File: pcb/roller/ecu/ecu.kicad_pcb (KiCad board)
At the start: 4 copper layers, 187.6 x 139.6 mm, 275 parts, among them J1 SWD, J2 NTC, J3 SS-12400-004, J4 NTC, J6 TE-776163-1, J7 TE-776087-1, K1 Relay_SPDT, K10 Relay_SPST-NO, K11 Relay_SPDT, K12 Relay_SPST-NO, K13 Relay_SPDT, K14 Relay_SPST-NO, K15 Relay_SPST-NO, K16 Relay_SPST-NO, K17 Relay_SPST-NO, K18 Relay_SPST-NO, K19 Relay_SPST-NO, K2 Relay_SPDT, K20 Relay_SPST-NO, K21 Relay_SPST-NO, K22 Relay_SPST-NO, K23 Relay_SPST-NO, K24 Relay_SPDT, K25 Relay_SPST-NO, K26 Relay_SPST-NO, K27 Relay_SPST-NO, K3 Relay_SPDT, K4 Relay_SPST-NO, K5 Relay_SPDT, K6 Relay_SPST-NO, K7 Relay_SPDT, K8 Relay_SPST-NO, K9 Relay_SPDT, Q1 BSN20, Q2 NVD5C684NLT4G, Q3 NVD5C684NLT4G, Q4 BC817, Q5 BSC065N06LS5, Q6 2N7002KQ-7, Q9 BSN20, SW1 SW_Push, T201 SM91071AL-E, U1 STM32H563ZITx, U10 UCC27517AQDBVRQ1, U11 UCC27517AQDBVRQ1, U12 INA240A1D, U13 SN65HVD230, U14 SN65HVD230, U15 ACPL-214-500E, U2 LM74700, U221 ATECC608C-SSHDA-T, U300 SN74AHCT541QPWRQ1, U301 TPIC6A595DWR, U302 TPIC6A595DWR, U303 TPIC6A595DWR, U304 TPIC6A595DWR, U4 LAN8742A, U5 USBLC6-4SC6, U6 INA240A1D, U7 SN74LVC1G14DBV, U8 MPQ4371GVE-1000-AEC1-P, U9 MPQ2178GQHE-AEC1-Z, Y1 32.768kHz, Y2 25MHz, Y3 25MHz

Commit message: Implement code changes to enhance functionality and improve performance
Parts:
- moved D12 144.9 mm to (439.2, 185.7)
- moved D4 144.9 mm to (442.5, 184.7)
- moved D8 144.9 mm to (451.7, 163.9)
- moved R102 144.9 mm to (448.8, 181.1)
- moved R111 144.9 mm to (451.3, 181.0)
- moved R112 144.9 mm to (451.3, 182.8)
- moved R117 144.9 mm to (451.7, 175.5)
- moved R87 144.9 mm to (446.2, 180.3)
- moved U15 144.9 mm to (439.5, 174.9)
- moved D15 144.9 mm to (445.4, 185.7)
- moved D17 144.9 mm to (442.1, 186.5)
- moved J2 144.9 mm to (451.3, 169.7)
- moved J4 144.9 mm to (443.2, 169.8)
- moved R109 144.9 mm to (442.8, 182.9)
- moved R110 144.9 mm to (439.5, 183.9)
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
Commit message: Add new resistor value and update used designators in ECU schematic
- Added a new resistor value of 0.8 to the list of available values.
- Updated the used designators to include J7 in the ECU schematic.
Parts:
- moved R95 224.2 mm to (245.3, 140.7), turned to -90 degrees
- moved R96 222.1 mm to (246.9, 140.7), turned to -90 degrees
- moved R103 220.6 mm to (251.6, 147.8), turned to -90 degrees
- moved R92 217.5 mm to (250.1, 140.7)
- moved C79 217.2 mm to (248.5, 140.7)
- moved R104 217.2 mm to (254.7, 147.8), turned to -90 degrees
- moved R93 216.4 mm to (250.1, 143.8), turned to -90 degrees
- moved R100 216.0 mm to (256.2, 147.8), turned to -90 degrees
- moved R99 214.7 mm to (256.9, 140.8), turned to -90 degrees
- moved C84 214.5 mm to (253.2, 147.8), turned to -90 degrees
- moved R88 213.6 mm to (264.1, 123.8)
- moved R101 210.8 mm to (259.2, 147.8), turned to -90 degrees
- moved R97 210.3 mm to (260.7, 147.8), turned to -90 degrees
- moved C83 208.8 mm to (257.7, 147.8), turned to -90 degrees
- moved D18 208.0 mm to (253.2, 144.3), turned to -90 degrees
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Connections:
- H1 pad 1: GND -> unconnected-(H1-Pad1)
- H2 pad 1: GND -> unconnected-(H2-Pad1)
- H3 pad 1: GND -> unconnected-(H3-Pad1)
- H4 pad 1: GND -> unconnected-(H4-Pad1)
- J7 pad 10: /04_CAN/CAN2_L -> /08_Sensors/OIL_LEVEL_IN
- J7 pad 11: /ESTOP_NC -> /04_CAN/CAN1_H
- J7 pad 12: +12V -> /04_CAN/CAN1_L
- J7 pad 13: /08_Sensors/OIL_LEVEL_IN -> /04_CAN/CAN2_H
- J7 pad 14: /08_Sensors/OIL_TEMP_IN -> /08_Sensors/WATER_LEVEL_IN
- J7 pad 15: /08_Sensors/WATER_LEVEL_IN -> /08_Sensors/ENGINE_SENSOR_IN
- J7 pad 16: /08_Sensors/SPEED_IN -> /04_CAN/CAN2_L
- J7 pad 17: /08_Sensors/ENGINE_SENSOR_IN -> /08_Sensors/SPEED_IN
- J7 pad 7: /04_CAN/CAN1_H -> +12V
- J7 pad 8: /04_CAN/CAN1_L -> /ESTOP_NC
- J7 pad 9: /04_CAN/CAN2_H -> /08_Sensors/OIL_TEMP_IN
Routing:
- net +12V: track 36.8 -> 246.2 mm, vias 57 -> 69
- net /ESTOP_NC: track 0.00 -> 128.9 mm, vias 0 -> 2
- net /04_CAN/CAN2_H: track 0.00 -> 106.7 mm
- net /04_CAN/CAN1_L: track 0.00 -> 98.9 mm
- net +5V: track 93.3 -> 188.1 mm, vias 5 -> 12
- net GND: track 123.1 -> 215.9 mm, vias 5 -> 41
- net /04_CAN/CAN1_H: track 0.00 -> 92.0 mm, vias 0 -> 1
- net /04_CAN/CAN2_L: track 0.00 -> 91.3 mm
- net PGND: track 65.7 -> 154.3 mm, vias 89 -> 95
- net /08_Sensors/ENGINE_SENSOR_IN: track 0.00 -> 86.2 mm, vias 0 -> 1
- net /08_Sensors/WATER_LEVEL_IN: track 0.00 -> 83.7 mm, vias 0 -> 1
- net /08_Sensors/OIL_LEVEL_IN: track 0.00 -> 78.4 mm, vias 0 -> 1
- net /08_Sensors/OIL_TEMP_IN: track 0.00 -> 67.7 mm
- net +3V3_ETH: track 0.00 -> 67.0 mm, vias 0 -> 2
- net /08_Sensors/SPEED_IN: track 0.00 -> 63.1 mm
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- added copper zone on In2.Cu, net +5V
- added copper zone on B.Cu, net GND
- added copper zone on F.Cu, net GND
- added copper zone on In1.Cu, net GND

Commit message: Implement feature X to enhance user experience and fix bug Y in module Z
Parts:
- moved C42 119.0 mm to (267.0, 209.4), turned to -90 degrees
- moved Y1 111.0 mm to (242.4, 188.1), turned to -90 degrees
- moved C6 109.6 mm to (250.0, 170.5), turned to -90 degrees
- moved R36 103.0 mm to (239.9, 209.7)
- moved C49 102.0 mm to (239.7, 186.8), turned to 180 degrees
- moved C50 101.0 mm to (239.7, 189.4), turned to 180 degrees
- moved R37 100.4 mm to (243.0, 206.5)
- moved C44 100.0 mm to (241.5, 206.5), turned to -90 degrees
- moved C43 97.8 mm to (239.9, 206.5), turned to -90 degrees
- moved C45 94.5 mm to (241.5, 209.7), turned to -90 degrees
- moved C46 93.5 mm to (243.0, 209.7), turned to -90 degrees
- moved C87 83.6 mm to (272.1, 214.4)
- moved J4 83.6 mm to (275.5, 211.7)
- moved R110 83.6 mm to (272.1, 206.4)
- moved C86 83.6 mm to (272.1, 208.0)
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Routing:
- net +3.3V: track 38.1 -> 174.0 mm, vias 0 -> 40
- net /02_MCU_Core/RMII_REF_CLK: track 0.00 -> 123.3 mm, vias 0 -> 2
- net /02_MCU_Core/RMII_MDIO: track 3.32 -> 122.2 mm, vias 0 -> 2
- net /02_MCU_Core/RMII_CRS_DV: track 0.00 -> 117.4 mm, vias 0 -> 2
- net /02_MCU_Core/RMII_TXD1: track 0.00 -> 116.8 mm, vias 0 -> 4
- net /02_MCU_Core/RMII_RXD0: track 0.00 -> 114.5 mm, vias 0 -> 2
- net /02_MCU_Core/RMII_RXD1: track 0.00 -> 112.3 mm, vias 0 -> 2
- net /02_MCU_Core/RMII_MDC: track 0.00 -> 112.2 mm, vias 0 -> 4
- net /02_MCU_Core/ENGINE_SENSOR_ADC: track 0.00 -> 112.0 mm, vias 0 -> 2
- net /02_MCU_Core/RMII_NRST: track 6.67 -> 110.5 mm
- net /02_MCU_Core/YV_BACK_I_ADC: track 0.00 -> 103.5 mm, vias 0 -> 2
- net GND: track 215.9 -> 316.2 mm, vias 41 -> 177
- net /02_MCU_Core/RMII_TX_EN: track 0.00 -> 98.7 mm, vias 0 -> 4
- net /02_MCU_Core/RMII_TXD0: track 0.00 -> 97.5 mm, vias 0 -> 4
- net /02_MCU_Core/SPEED_PULSE: track 0.00 -> 96.6 mm, vias 0 -> 2
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- added copper zone on In2.Cu, net +3.3V

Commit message: Implement new feature for user authentication and improve error handling
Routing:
- net +3.3V: track 174.0 -> 175.4 mm, vias 40 -> 38
- net GND: track 316.2 -> 316.4 mm, vias 177 -> 185

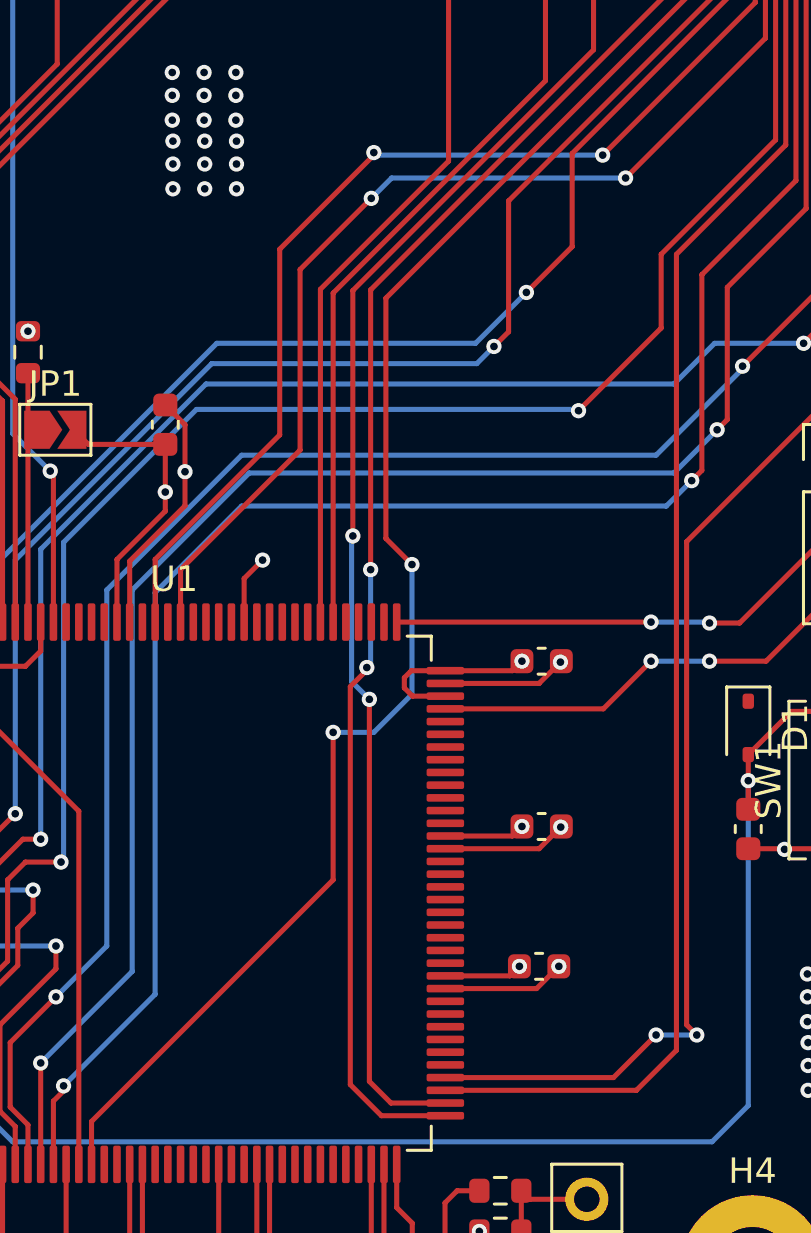
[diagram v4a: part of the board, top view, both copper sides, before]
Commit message: Update used_designators in ecu.kicad_pro to include resistors R113-115
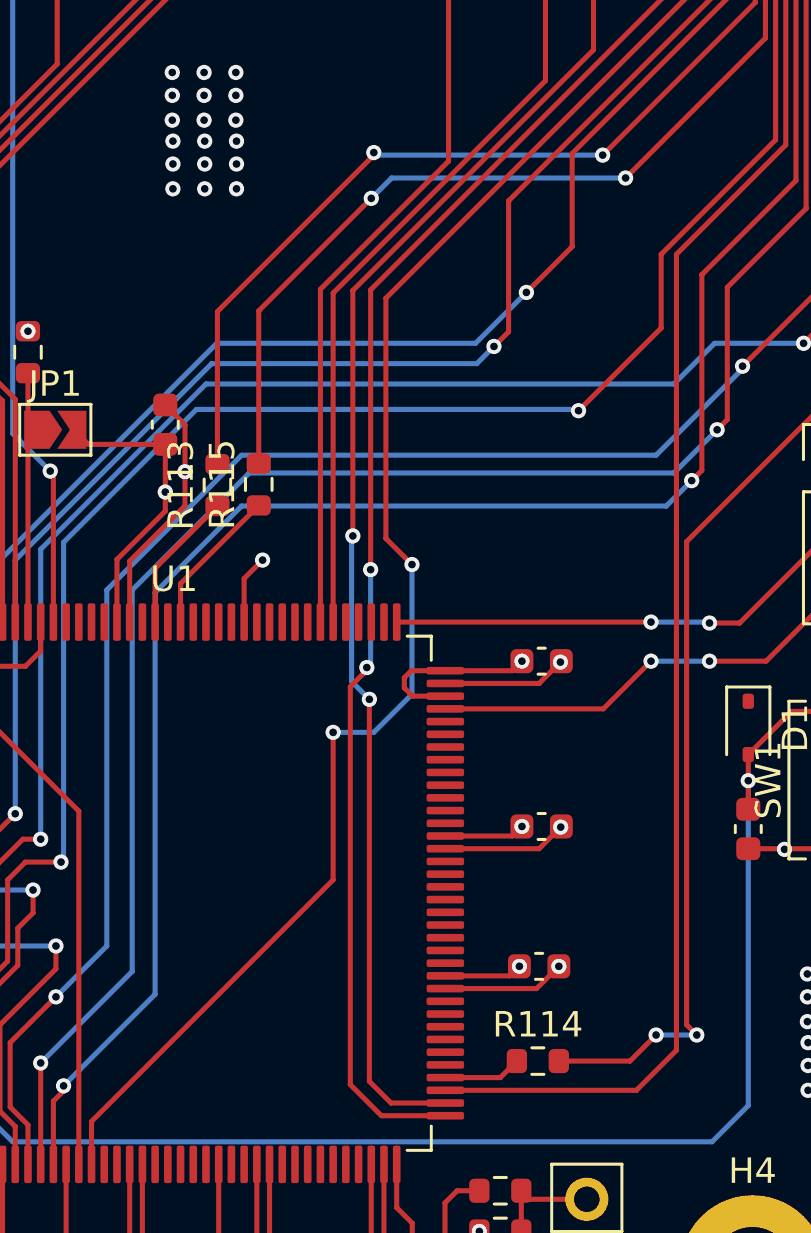
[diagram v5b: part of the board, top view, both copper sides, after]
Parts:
- added R113: 33R, Resistor_SMD:R_0603_1608Metric, F.Cu at (260.9, 177.1)
- added R114: 33R, Resistor_SMD:R_0603_1608Metric, F.Cu at (273.6, 199.7)
- added R115: 33R, Resistor_SMD:R_0603_1608Metric, F.Cu at (262.6, 177.1)
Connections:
- U4 pad 16: /02_MCU_Core/RMII_TX_EN -> Net-(U4-TXEN)
- U4 pad 17: /02_MCU_Core/RMII_TXD0 -> Net-(U4-TXD0)
- U4 pad 18: /02_MCU_Core/RMII_TXD1 -> Net-(U4-TXD1)
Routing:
- net /02_MCU_Core/RMII_TXD1: track 116.8 -> 3.08 mm, vias 4 -> 0
- net Net-(U4-TXD1): track 0.00 -> 112.0 mm, vias 0 -> 4
- net /02_MCU_Core/RMII_TX_EN: track 98.7 -> 5.86 mm, vias 4 -> 0
- net /02_MCU_Core/RMII_TXD0: track 97.5 -> 5.58 mm, vias 4 -> 0
- net Net-(U4-TXEN): track 0.00 -> 91.2 mm, vias 0 -> 4
- net Net-(U4-TXD0): track 0.00 -> 90.3 mm, vias 0 -> 4

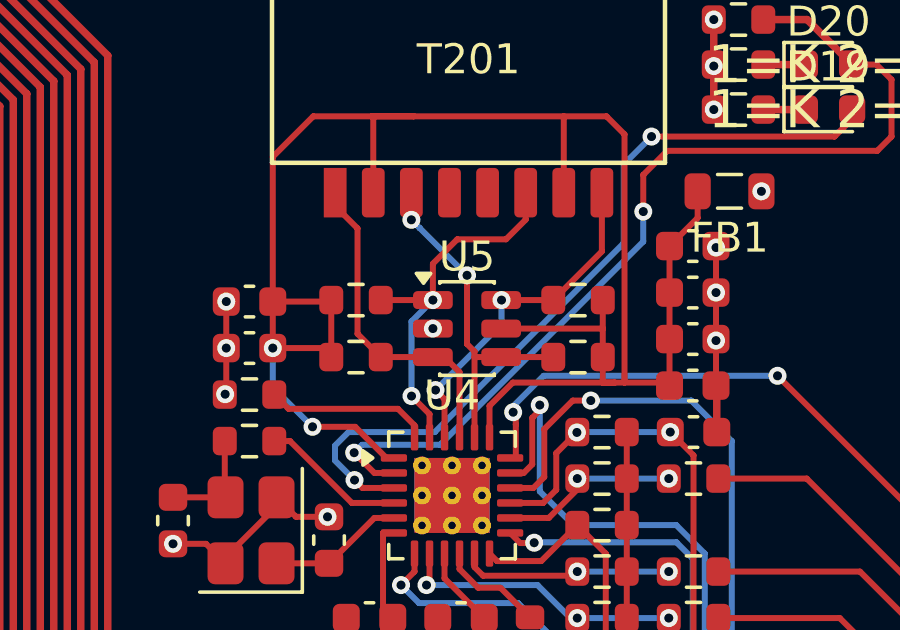
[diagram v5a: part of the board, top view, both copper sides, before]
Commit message: Add Ethernet segments and tuning pattern to ECU PCB layout
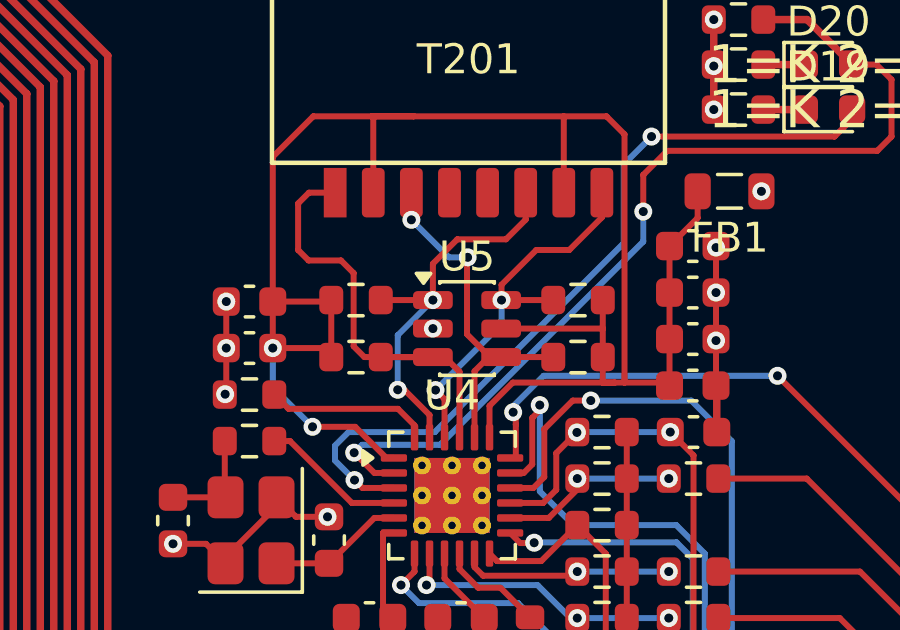
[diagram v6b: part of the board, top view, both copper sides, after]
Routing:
- net /03_Ethernet/TD_P: track 11.1 -> 17.1 mm
- net /03_Ethernet/RD_N: track 11.6 -> 13.0 mm
- net /03_Ethernet/TD_N: track 11.9 -> 12.6 mm
- net /03_Ethernet/RD_P: track 12.5 -> 13.0 mm
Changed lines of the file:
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@@
 	)
 	(segment
+		(start 269.87 104.275)
+		(end 269.85 104.295)
+		(width 0.2)
+		(layer "F.Cu")
+		(net "/03_Ethernet/TD_N")
+	)
+	(segment
 		(start 271 107.6)
 		(end 270.9875 107.6)
@@
 	)
 	(segment
+		(start 269.85 106.84)
+		(end 270.61 107.6)
+		(width 0.2)
+		(layer "F.Cu")
+		(net "/03_Ethernet/TD_N")
+	)
+	(segment
 		(start 271.0375 107.6)
 		(end 270.95 107.6)
@@
 	)
 	(segment
-		(start 270.1 107.415552)
-		(end 269.85 107.165552)
+		(start 269.85 106.176499)
+		(end 269.85 106.784965)
 		(width 0.2)
 		(layer "F.Cu")
@@
 	)
 	(segment
-		(start 269.85 104.875)
-		(end 269.85 107.165552)
+		(start 272.725 107.6)
+		(end 271 107.6)
 		(width 0.2)
 		(layer "F.Cu")
@@
 	)
 	(segment
-		(start 270.1 107.6)
-		(end 270.1 107.415552)
+		(start 269.85 104.295)
+		(end 269.85 106.176499)
+		(width 0.2)
+		(layer "F.Cu")
+		(net "/03_Ethernet/TD_N")
+	)
+	(segment
+		(start 269.85 106.784965)
+		(end 269.85 106.84)
 		(width 0.2)
 		(layer "F.Cu")
@@
 	(segment
 		(start 270.9875 107.6)
-		(end 270.1 107.6)
+		(end 270.57 107.6)
 		(width 0.2)
 		(layer "F.Cu")
@@
 	)
 	(segment
-		(start 272.725 107.6)
-		(end 271 107.6)
+		(start 270.61 107.6)
+		(end 270.9875 107.6)
 		(width 0.2)
 		(layer "F.Cu")
@@
 	)
 	(segment
-		(start 270.1 110.275)
-		(end 270.1 107.6)
+		(start 270.1 108.07)
+		(end 270.1 110.275)
+		(width 0.2)
+		(layer "F.Cu")
+		(net "/03_Ethernet/TD_N")
+	)
+	(segment
+		(start 270.57 107.6)
+		(end 270.1 108.07)
 		(width 0.2)
 		(layer "F.Cu")
@@
 	)
 	(via
-		(at 269.85 104.875)
+		(at 269.87 104.275)
 		(size 0.6)
 		(drill 0.3)
@@
 	)
 	(segment
-		(start 268.27 103.3)
-		(end 268.275 103.3)
+		(start 269.87 104.275)
+		(end 269.245 104.275)
 		(width 0.2)
 		(layer "B.Cu")
@@
 	)
 	(segment
-		(start 268.275 103.3)
-		(end 269.85 104.875)
+		(start 269.245 104.275)
+		(end 267.995 103.025)
 		(width 0.2)
 		(layer "B.Cu")
@@
 	)
 	(segment
-		(start 267.995 103.025)
-		(end 268.27 103.3)
+		(start 264.22 104.03)
+		(end 264.57 104.38)
 		(width 0.2)
-		(layer "B.Cu")
-		(net "/03_Ethernet/TD_N")
+		(layer "F.Cu")
+		(net "/03_Ethernet/TD_P")
 	)
 	(segment
@@
 	)
 	(segment
-		(start 266.2 103.31)
-		(end 266.2 106.825)
+		(start 266.975 107.6)
+		(end 268.7125 107.6)
 		(width 0.2)
 		(layer "F.Cu")
@@
 	)
 	(segment
-		(start 265.455 102.12)
-		(end 265.455 102.565)
+		(start 266.07 107.24)
+		(end 266.43 107.6)
+		(width 0.2)
+		(layer "F.Cu")
+		(net "/03_Ethernet/TD_P")
+	)
+	(segment
+		(start 264.57 104.38)
+		(end 265.65 104.38)
+		(width 0.2)
+		(layer "F.Cu")
+		(net "/03_Ethernet/TD_P")
+	)
+	(segment
+		(start 269.6 110.275)
+		(end 269.6 108.09)
 		(width 0.2)
 		(layer "F.Cu")
@@
 	)
 	(segment
-		(start 269.1 107.6)
+		(start 269.6 108.09)
+		(end 269.11 107.6)
+		(width 0.2)
+		(layer "F.Cu")
+		(net "/03_Ethernet/TD_P")
+	)
+	(segment
+		(start 266.43 107.6)
 		(end 268.7125 107.6)
 		(width 0.2)
@@
 	)
 	(segment
-		(start 269.6 108.1)
-		(end 269.1 107.6)
+		(start 264.58 102.12)
+		(end 264.22 102.48)
+		(width 0.2)
+		(layer "F.Cu")
+		(net "/03_Ethernet/TD_P")
+	)
+	(segment
+		(start 269.11 107.6)
+		(end 268.7125 107.6)
+		(width 0.2)
+		(layer "F.Cu")
+		(net "/03_Ethernet/TD_P")
+	)
+	(segment
+		(start 265.455 102.12)
+		(end 264.58 102.12)
 		(width 0.2)
 		(layer "F.Cu")
@@
 	)
 	(segment
-		(start 269.6 110.275)
-		(end 269.6 108.1)
+		(start 265.65 104.38)
+		(end 266.07 104.8)
 		(width 0.2)
 		(layer "F.Cu")
@@
 	)
 	(segment
-		(start 266.2 106.825)
-		(end 266.975 107.6)
+		(start 264.22 102.48)
+		(end 264.22 104.03)
 		(width 0.2)
 		(layer "F.Cu")
@@
 	)
 	(segment
-		(start 265.455 102.565)
-		(end 266.2 103.31)
+		(start 266.07 104.8)
+		(end 266.07 107.24)
 		(width 0.2)
 		(layer "F.Cu")
@@
 	)
 	(segment
+		(start 271 105.19)
+		(end 271 105.7)
+		(width 0.2)
+		(layer "F.Cu")
+		(net "/03_Ethernet/RD_N")
+	)
+	(segment
 		(start 272.7625 105.7)
 		(end 272.725 105.7)
@@
 	)
 	(segment
-		(start 272.725 105.7)
-		(end 274.345 104.08)
+		(start 273.26 104.03)
+		(end 272.16 104.03)
 		(width 0.2)
 		(layer "F.Cu")
@@
 	)
 	(segment
-		(start 272.725 105.7)
-		(end 271 105.7)
+		(start 274.345 102.945)
+		(end 273.26 104.03)
 		(width 0.2)
 		(layer "F.Cu")
@@
 	)
 	(segment
-		(start 269.1 109)
-		(end 269.1 110.275)
+		(start 272.16 104.03)
+		(end 271 105.19)
+		(width 0.2)
+		(layer "F.Cu")
+		(net "/03_Ethernet/RD_N")
+	)
+	(segment
+		(start 274.345 102.12)
+		(end 274.345 102.945)
+		(width 0.2)
+		(layer "F.Cu")
+		(net "/03_Ethernet/RD_N")
+	)
+	(segment
+		(start 272.725 105.7)
+		(end 271 105.7)
 		(width 0.2)
 		(layer "F.Cu")
@@
 	)
 	(segment
-		(start 274.345 104.08)
-		(end 274.345 102.12)
+		(start 269.1 109)
+		(end 269.1 110.275)
 		(width 0.2)
 		(layer "F.Cu")
@@
 	)
 	(segment
-		(start 268.6 109.5)
-		(end 268 108.9)
+		(start 267.54 108.69)
+		(end 267.56 108.71)
+		(width 0.2)
+		(layer "F.Cu")
+		(net "/03_Ethernet/RD_P")
+	)
+	(segment
+		(start 267.78 108.71)
+		(end 268.6 109.53)
 		(width 0.2)
 		(layer "F.Cu")
@@
 	)
 	(segment
-		(start 268.6 110.275)
-		(end 268.6 109.5)
+		(start 267.56 108.71)
+		(end 267.78 108.71)
 		(width 0.2)
 		(layer "F.Cu")
@@
 	)
 	(segment
+		(start 268.6 109.53)
+		(end 268.6 110.275)
+		(width 0.2)
+		(layer "F.Cu")
+		(net "/03_Ethernet/RD_P")
+	)
+	(segment
 		(start 268.7125 104.4875)
 		(end 269.525 103.675)
@@
 	)
 	(via
-		(at 268 108.9)
+		(at 267.54 108.69)
 		(size 0.6)
 		(drill 0.3)
@@
 	)
 	(segment
-		(start 268 108.9)
-		(end 268 106.4125)
+		(start 267.54 108.69)
+		(end 267.54 106.8725)
 		(width 0.2)
 		(layer "B.Cu")
@@
 	)
 	(segment
-		(start 268 106.4125)
+		(start 267.54 106.8725)
 		(end 268.7125 105.7)
 		(width 0.2)
@@
 		)
 	)
+	(generated
+		(type tuning_pattern)
+		(name "Tuning Pattern")
+		(layer "F.Cu")
+		(base_line
+			(pts
+				(xy 269.85 106.176499) (xy 269.85 106.784965)
+			)
+		)
+		(base_line_coupled
+			(pts
+				(xy 269.1 107.6) (xy 269.128329 107.628329)
+			)
+		)
+		(corner_radius_percent 80)
+		(end
+			(xy 269.85 106.784965)
+		)
+		(initial_side "right")
+		(is_time_domain no)
+		(last_diff_pair_gap 0.18)
+		(last_netname "/03_Ethernet/TD_N")
+		(last_status "too_long")
+		(last_track_width 0.2)
+		(last_tuning_length 2.880724)
+		(max_amplitude 1)
+		(min_amplitude 0.2)
+		(min_spacing 0.6)
+		(origin
+			(xy 269.85 106.176499)
+		)
+		(override_custom_rules no)
+		(rounded yes)
+		(single_sided no)
+		(target_delay 1000000)
+		(target_delay_max 1000000)
+		(target_delay_min 0)
+		(target_length 1000000)
+		(target_length_max 1000000)
+		(target_length_min 0)
+		(target_skew 0)
+		(target_skew_max 0.1)
+		(target_skew_min -0.1)
+		(tuning_mode "diff_pair_skew")
+		(members "57624d95-2b53-4996-a6d4-0b86e549357a")
+	)
 	(embedded_fonts no)
